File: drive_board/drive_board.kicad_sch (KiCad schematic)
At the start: 12 parts, among them J1 RJ45_LED_Shielded, J3 Conn_01x02_Pin, J4 Conn_01x02_Pin, J5 Conn_01x02_Pin, U3 SN65HVD232

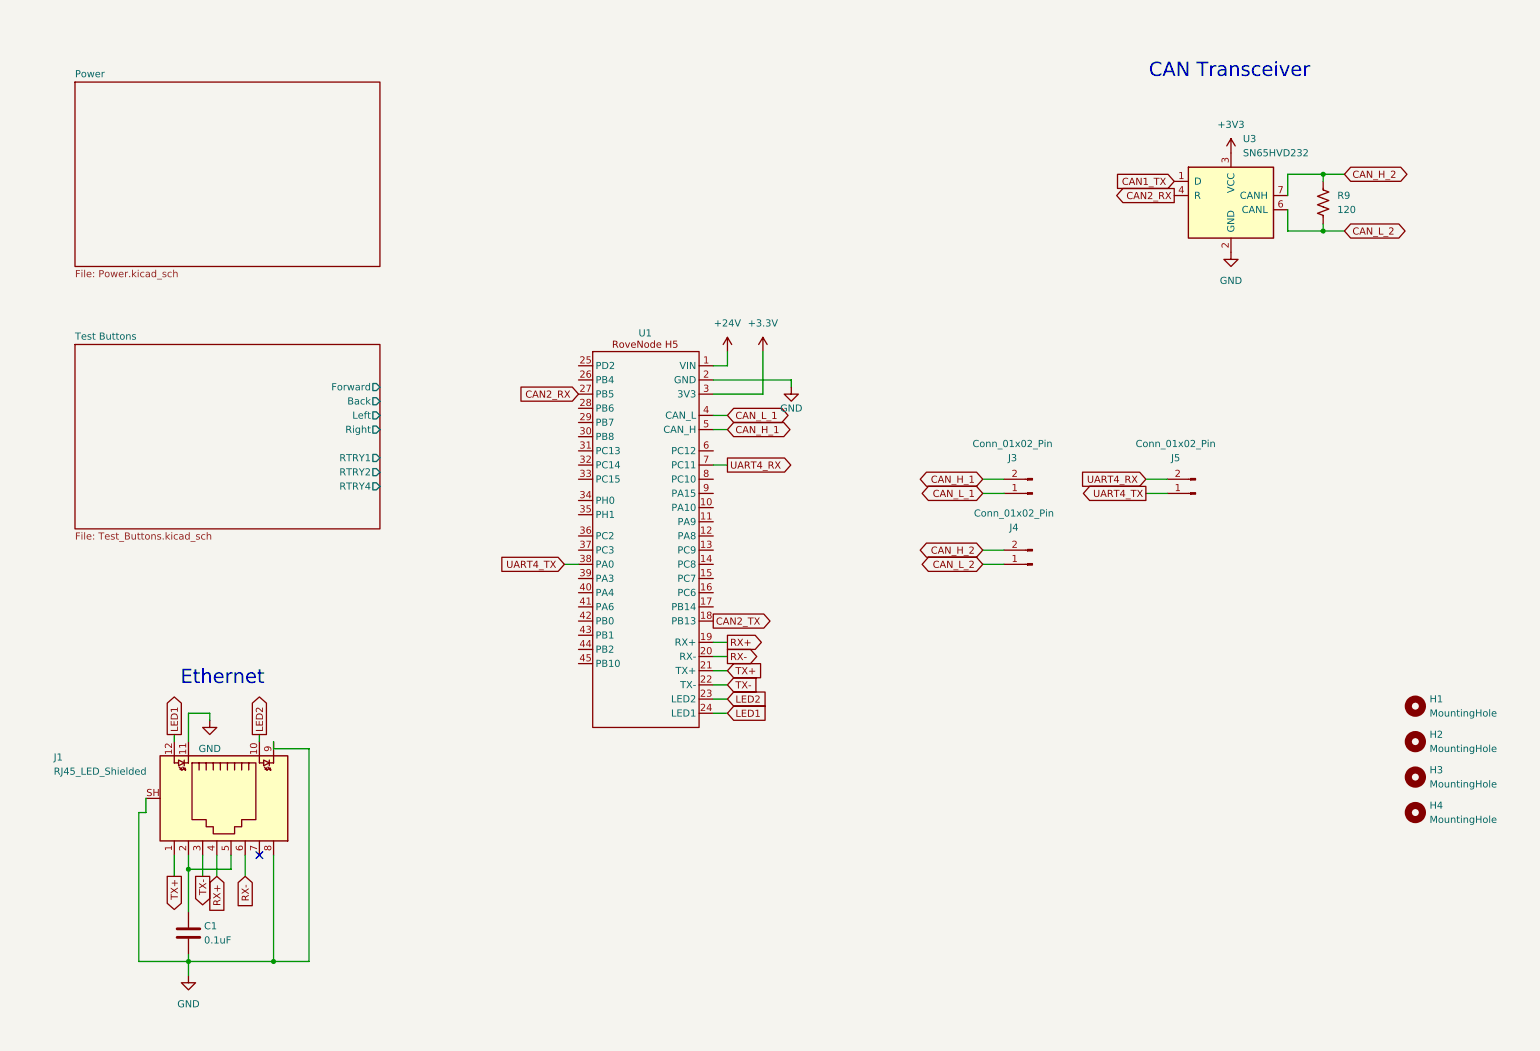
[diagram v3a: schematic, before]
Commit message: Removed terminating resistors, assigned more pins, more connectors for CAN busses.
- Assigned GPIO inputs for test buttons and rotary encoder. Hopefully that works ._.
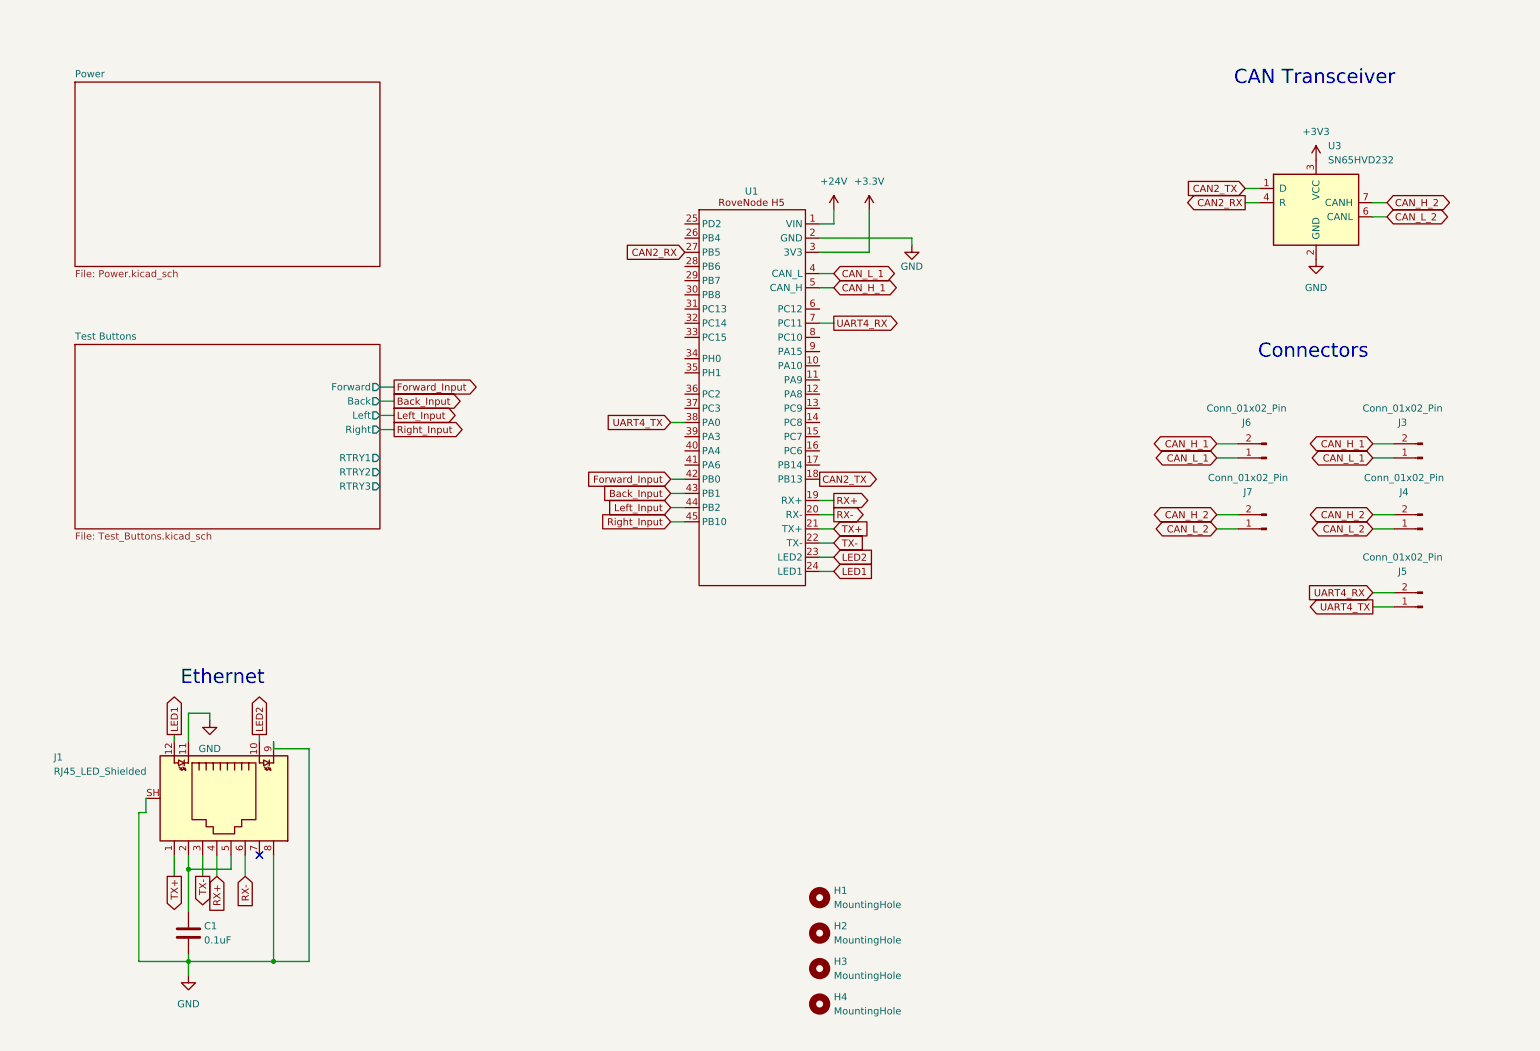
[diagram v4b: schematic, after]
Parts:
- removed R9: 120, Resistor_SMD:R_0603_1608Metric_Pad0.98x0.95mm_HandSolder, symbol Device:R_US
- added J6, J7: Conn_01x02_Pin, Package_DFN_QFN:QFN-20-1EP_5x5mm_P0.65mm_EP3.35x3.35mm, symbol Connector:Conn_01x02_Pin
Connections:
- net CAN1_TX is gone; now on net CAN2_TX: U3.1 (D)
- net CAN_H_1: now also J6.2 (Pin_2)
- net CAN_H_2: now also J7.2 (Pin_2)
- net CAN_L_1: now also J6.1 (Pin_1)
- net CAN_L_2: now also J7.1 (Pin_1)
- net Forward_Input: now reaches U1.42 (PB0)
- net Back_Input: now reaches U1.43 (PB1)
- net Left_Input: now reaches U1.44 (PB2)
- net Right_Input: now reaches U1.45 (PB10)
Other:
- sheet Test Buttons ports: added RTRY3; removed RTRY4
- note added: "Connectors"
- moved on the sheet: H1, H2, H3, H4, J3, J4, J5, U1, U3

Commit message: Finish schematic
- Finished requirements
- Cleaned up and organized some stuff
- Can still clean up a little more
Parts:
- removed J5: Conn_01x02_Pin, Package_DFN_QFN:QFN-20-1EP_5x5mm_P0.65mm_EP3.35x3.35mm, symbol Connector:Conn_01x02_Pin
- added J10: Conn_01x04_Pin, Package_DIP:DIP-20_W7.62mm, symbol Connector:Conn_01x04_Pin
- added J6, J7, J8, J9: Conn_01x02_Pin, Package_DFN_QFN:QFN-20-1EP_5x5mm_P0.65mm_EP3.35x3.35mm, symbol Connector:Conn_01x02_Pin
- renumbered J6 to J2, J7 to J4, J4 to J5
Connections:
- net +24V: now also J10.4 (Pin_4)
- net GND: now also J10.1 (Pin_1), J6.1 (Pin_1), J7.1 (Pin_1), J8.1 (Pin_1), J9.1 (Pin_1)
- net UART4_RX: now also J10.3 (Pin_3)
- net UART4_TX: now also J10.2 (Pin_2)
- net RTRY4: now reaches U1.10 (PA10)
- net RTRY2: now reaches U1.11 (PA9)
- net RTRY1: now reaches U1.12 (PA8)
- net LS4: now reaches U1.13 (PC9)
- net LS4: now also J9.2 (Pin_2)
- net LS3: now reaches U1.14 (PC8)
- net LS3: now also J8.2 (Pin_2)
- net LS2: now reaches U1.15 (PC7)
- net LS2: now also J7.2 (Pin_2)
- net LS1: now reaches U1.16 (PC6)
- net LS1: now also J6.2 (Pin_2)
- net FLMOT_T: now reaches U1.28 (PB6)
- net FLMOT_W: now reaches U1.29 (PB7)
- net FRMOT_T: now reaches U1.30 (PB8)
- net FRMOT_W: now reaches U1.31 (PC13)
- net BLMOT_T: now reaches U1.32 (PC14)
- net BLMOT_W: now reaches U1.33 (PC15)
- net BRMOT_T: now reaches U1.34 (PH0)
- net BRMOT_W: now reaches U1.35 (PH1)
- no-connect marks 1 -> 12
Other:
- sheet Test Buttons ports: added BLMOT_T, BLMOT_W, BRMOT_T, BRMOT_W, FLMOT_T, FLMOT_W, FRMOT_T, FRMOT_W, RTRY4; removed RTRY3
- note added: "Mounting Holes"
- note added: "Power"
- note added: "RoveNode"
- note added: "Test Buttons"
- moved on the sheet: C1, H1, H2, H3, H4, J1, J2, J3, J4, J5, U1, U3

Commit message: Organize schematic stuff
- Did new stuff lol!1! 67
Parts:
- renumbered J9 to J10, J10 to J11, J1 to J2, J2 to J3, J3 to J4, J4 to J5, J5 to J6, J6 to J7, J7 to J8, J8 to J9, U3 to U2
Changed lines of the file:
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@@
 		(in_pos_files yes)
 		(dnp no)
-		(property "Reference" "J9"
+		(property "Reference" "J10"
 			(at 263.398 83.566 0)
 			(show_name no)
@@
 			(project "drive_board"
 				(path "/8a12bcce-bfce-42ac-b1ed-7dac1a4a0fe5"
-					(reference "J9")
+					(reference "J10")
 					(unit 1)
 				)
@@
 		(in_pos_files yes)
 		(dnp no)
-		(property "Reference" "J4"
+		(property "Reference" "J5"
 			(at 235.458 46.736 0)
 			(show_name no)
@@
 			(project "drive_board"
 				(path "/8a12bcce-bfce-42ac-b1ed-7dac1a4a0fe5"
-					(reference "J4")
+					(reference "J5")
 					(unit 1)
 				)
@@
 		(in_pos_files yes)
 		(dnp no)
-		(property "Reference" "J5"
+		(property "Reference" "J6"
 			(at 263.398 46.736 0)
 			(show_name no)
@@
 			(project "drive_board"
 				(path "/8a12bcce-bfce-42ac-b1ed-7dac1a4a0fe5"
-					(reference "J5")
+					(reference "J6")
 					(unit 1)
 				)
@@
 		(in_pos_files yes)
 		(dnp no)
-		(property "Reference" "J8"
+		(property "Reference" "J9"
 			(at 235.458 83.566 0)
 			(show_name no)
@@
 			(project "drive_board"
 				(path "/8a12bcce-bfce-42ac-b1ed-7dac1a4a0fe5"
-					(reference "J8")
+					(reference "J9")
 					(unit 1)
 				)
@@
 		(dnp no)
 		(fields_autoplaced yes)
-		(property "Reference" "U3"
+		(property "Reference" "U2"
 			(at 140.5733 152.4 0)
 			(show_name no)
@@
 			(project "drive_board"
 				(path "/8a12bcce-bfce-42ac-b1ed-7dac1a4a0fe5"
-					(reference "U3")
+					(reference "U2")
 					(unit 1)
 				)
@@
 		(in_pos_files yes)
 		(dnp no)
-		(property "Reference" "J3"
+		(property "Reference" "J4"
 			(at 263.144 34.29 0)
 			(show_name no)
@@
 			(project "drive_board"
 				(path "/8a12bcce-bfce-42ac-b1ed-7dac1a4a0fe5"
-					(reference "J3")
+					(reference "J4")
 					(unit 1)
 				)
@@
 		(in_pos_files yes)
 		(dnp no)
-		(property "Reference" "J7"
+		(property "Reference" "J8"
 			(at 263.398 70.866 0)
 			(show_name no)
@@
 			(project "drive_board"
 				(path "/8a12bcce-bfce-42ac-b1ed-7dac1a4a0fe5"
-					(reference "J7")
+					(reference "J8")
 					(unit 1)
 				)
@@
 		(in_pos_files yes)
 		(dnp no)
-		(property "Reference" "J6"
+		(property "Reference" "J7"
 			(at 235.458 70.866 0)
 			(show_name no)
@@
 			(project "drive_board"
 				(path "/8a12bcce-bfce-42ac-b1ed-7dac1a4a0fe5"
-					(reference "J6")
+					(reference "J7")
 					(unit 1)
 				)
@@
 		(in_pos_files yes)
 		(dnp no)
-		(property "Reference" "J10"
+		(property "Reference" "J11"
 			(at 262.382 114.3 0)
 			(show_name no)
@@
 			(project "drive_board"
 				(path "/8a12bcce-bfce-42ac-b1ed-7dac1a4a0fe5"
-					(reference "J10")
+					(reference "J11")
 					(unit 1)
 				)
@@
 		(in_pos_files yes)
 		(dnp no)
-		(property "Reference" "J1"
+		(property "Reference" "J2"
 			(at 26.67 150.114 90)
 			(show_name no)
@@
 			(project "drive_board"
 				(path "/8a12bcce-bfce-42ac-b1ed-7dac1a4a0fe5"
-					(reference "J1")
+					(reference "J2")
 					(unit 1)
 				)
@@
 		(in_pos_files yes)
 		(dnp no)
-		(property "Reference" "J2"
+		(property "Reference" "J3"
 			(at 235.204 34.29 0)
 			(show_name no)
@@
 			(project "drive_board"
 				(path "/8a12bcce-bfce-42ac-b1ed-7dac1a4a0fe5"
-					(reference "J2")
-					(unit 1)
-				)
+					(reference "J3")
+					(unit 1)
+				)

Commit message: Adjust according to schematic review
- Added some pull down resistors and such
- Lowkey forgot because I forgot to commit and am a couple days late.
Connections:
- net GND: now also J11.3 (Pin_3); no longer J11.1 (Pin_1)
- net UART4_RX: now also J11.2 (Pin_2); no longer J11.3 (Pin_3)
- net UART4_TX: now also J11.1 (Pin_1); no longer J11.2 (Pin_2)

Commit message: Change Testing Control Scheme
- Removed testing D-pad.
- Removed rotary encoder.
- Added two complete (maybe) joystick potentiometer circuits.
- Added dip switch (no circuit).
- Assigned some footprints.
- Grounded mounting holes.
- Added CAN transceiver terminating resistor (footprint only).
- Other stuff I prob forgot.
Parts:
- removed H1, H2, H3, H4: MountingHole, MRDT_Shields:RoveNode_H5, symbol Mechanical:MountingHole
- added C3: 10uF, symbol Device:C
- added C4: 0.1uF, symbol Device:C
- added H1, H2, H3, H4: MountingHole_Pad, symbol Mechanical:MountingHole_Pad
- added R24: 120, Resistor_SMD:R_0603_1608Metric_Pad0.98x0.95mm_HandSolder, symbol Device:R_US
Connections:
- net +3V3: now also C3.1, C4.1
- net BLMOT_T: no longer U1.32 (PC14)
- net BLMOT_W: no longer U1.33 (PC15)
- net BRMOT_T: no longer U1.34 (PH0)
- net BRMOT_W: no longer U1.35 (PH1)
- net CAN_H_2: now also R24.1
- net CAN_L_2: now also R24.2
- net FLMOT_T: no longer U1.28 (PB6)
- net FLMOT_W: no longer U1.29 (PB7)
- net FRMOT_T: no longer U1.30 (PB8)
- net FRMOT_W: no longer U1.31 (PC13)
- net GND: now also C3.2, C4.2, H1.1, H2.1, H3.1, H4.1
- net JYSTK2_VERT: now reaches U1.39 (PA3)
- net JYSTK2_HORIZ: now reaches U1.40 (PA4)
- net JYSTK2_PRS: now reaches U1.41 (PA6)
- net RTRY1 renamed JYSTK1_PRS
- net RTRY2 renamed JYSTK1_HORIZ
- net RTRY4 renamed JYSTK1_VERT
- new net BCK_LFT_TURN_MOT: U1.32 (PC14)
- new net BCK_LFT_WHL_MOT: U1.33 (PC15)
- new net BCK_RGHT_TURN_MOT: U1.34 (PH0)
- new net BCK_RGHT_WHL_MOT: U1.35 (PH1)
- new net FNT_LFT_TURN_MOT: U1.28 (PB6)
- new net FNT_LFT_WHL_MOT: U1.29 (PB7)
- new net FNT_RGHT_TURN_MOT: U1.30 (PB8)
- new net FNT_RGHT_WHL_MOT: U1.31 (PC13)
- no-connect marks 12 -> 9
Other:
- sheet Test Buttons ports: added JYSTK1_HORIZ, JYSTK1_PRS, JYSTK1_VERT, JYSTK2_HORIZ, JYSTK2_PRS, JYSTK2_VERT; removed Back, Forward, Left, RTRY1, RTRY2, RTRY4, Right
- note added: "Test Controls"
- note removed: "Test Buttons"
- moved on the sheet: J10, J11, J3, J4, J5, J6, J7, J8, J9, U1, U2
